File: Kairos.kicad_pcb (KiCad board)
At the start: 2 copper layers, 285 x 94.6 mm, 133 parts, among them Q1 NSS40301MZ4T1G, U1 ATMEGA32U2-AU, Y1 Crystal

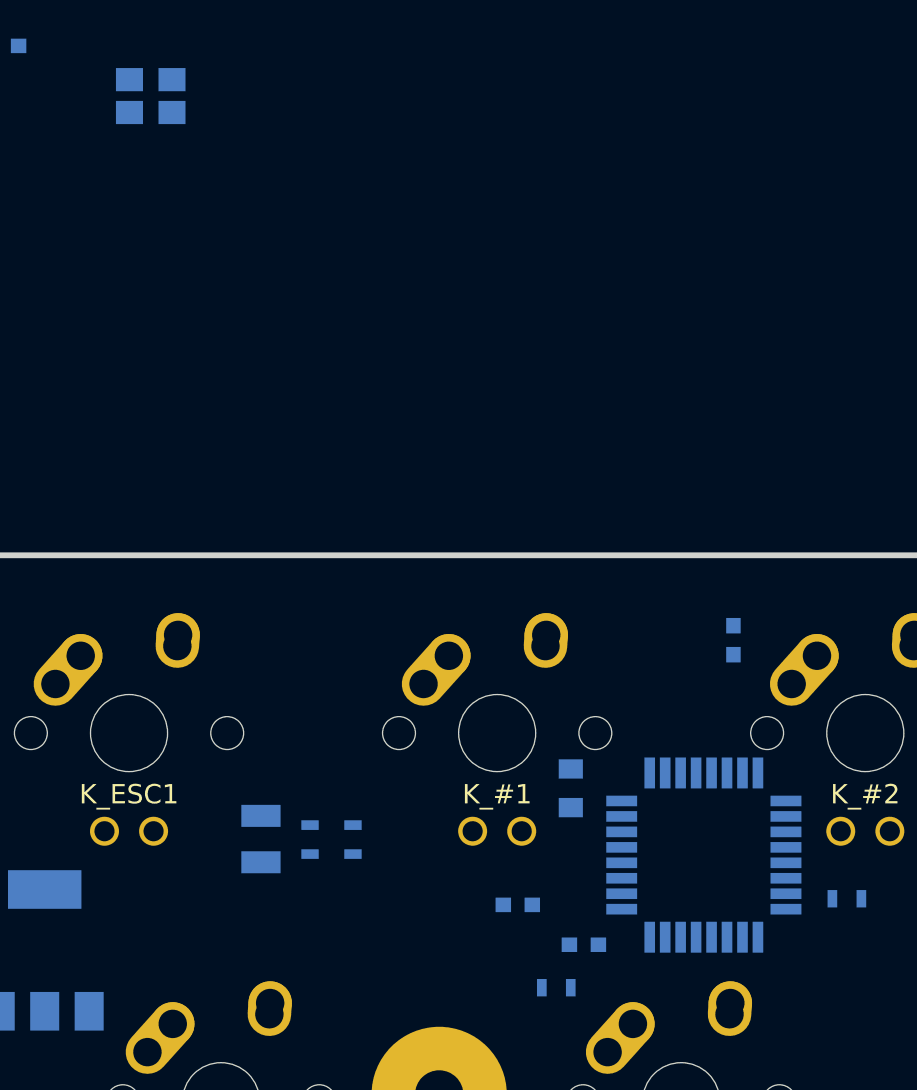
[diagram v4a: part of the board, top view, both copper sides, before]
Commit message: Seems like the crystal pinout is incorrect
Commit before fix for the sake of safety
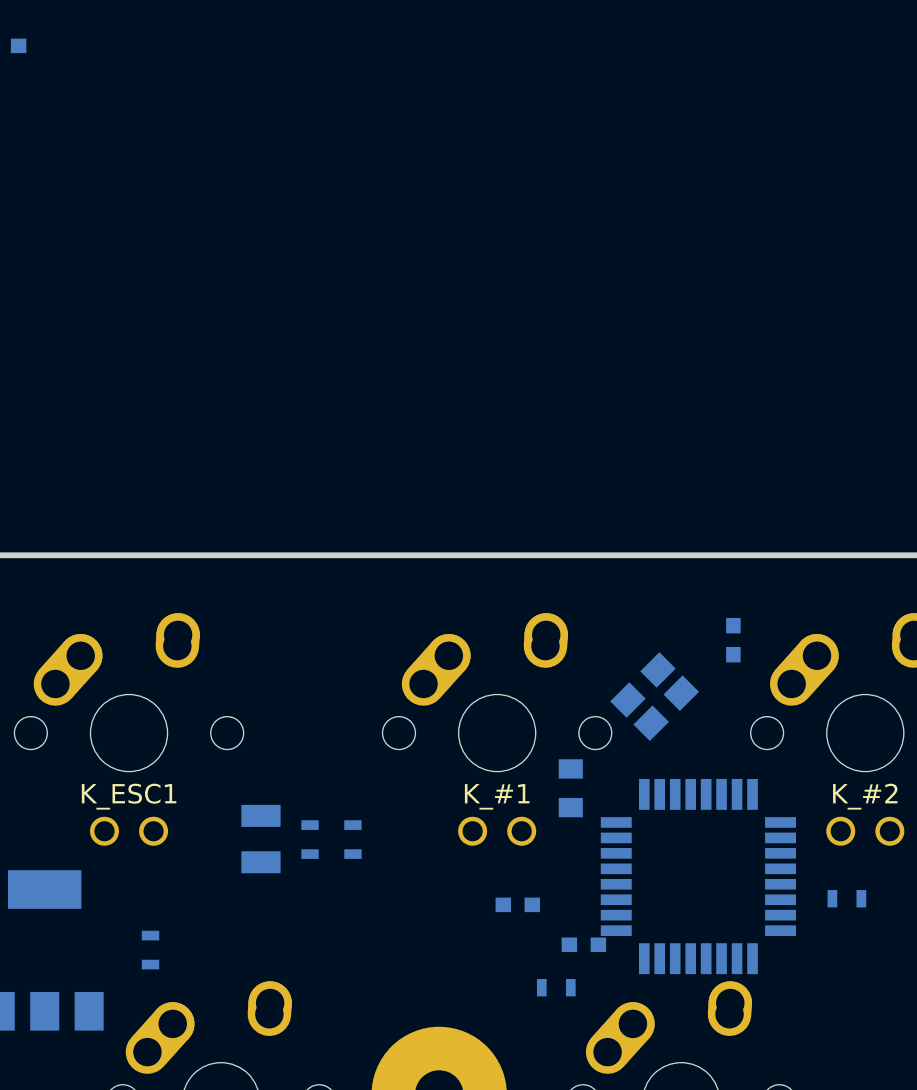
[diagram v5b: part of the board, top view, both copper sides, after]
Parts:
- added R5: 1.5k, Resistors_SMD:R_0603, B.Cu at (15.4, 42.2)
- moved Y1 40.6 mm to (41.5, 29.1), turned to 45 degrees
- moved U1 1.15 mm to (43.8, 38.4)
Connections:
- U1 pad 21: Net-(Q1-Pad1) -> Net-(R5-Pad2)
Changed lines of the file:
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@@
 (kicad_pcb (version 4) (host pcbnew 4.0.6)
   (general
-    (links 590)
-    (no_connects 345)
+    (links 591)
+    (no_connects 347)
     (area 0 0 0 0)
     (thickness 1.6)
@@
     (tracks 0)
     (zones 0)
-    (modules 133)
-    (nets 181)
+    (modules 134)
+    (nets 182)
   )
   (page A4)
@@
   (net 179 "Net-(U1-Pad25)")
   (net 180 "Net-(U1-Pad26)")
+  (net 181 "Net-(R5-Pad2)")
   (net_class Default "This is the default net class."
     (clearance 0.2)
@@
     (add_net "Net-(R3-Pad1)")
     (add_net "Net-(R4-Pad1)")
+    (add_net "Net-(R5-Pad2)")
     (add_net "Net-(U1-Pad10)")
     (add_net "Net-(U1-Pad11)")
@@
   )
   (module Housings_QFP:TQFP-32_7x7mm_Pitch0.8mm (layer B.Cu)
-    (at 44.03125 37.27 270)
+    (at 43.75125 38.38125 270)
     (descr "32-Lead Plastic Thin Quad Flatpack (PT) - 7x7x1.0 mm Body, 2.00 mm [TQFP] (see Microchip Packaging Specification 00000049BS.pdf)")
     (tags "QFP 0.8")
@@
       (net 176 RGBLED))
     (pad 21 smd rect (at 4.25 0.4 270) (size 1.6 0.55) (layers B.Cu B.Paste B.Mask)
-      (net 161 "Net-(Q1-Pad1)"))
+      (net 181 "Net-(R5-Pad2)"))
     (pad 22 smd rect (at 4.25 1.2 270) (size 1.6 0.55) (layers B.Cu B.Paste B.Mask)
       (net 177 "Net-(U1-Pad22)"))
@@
   )
   (module Crystals:Crystal_SMD_3225-4pin_3.2x2.5mm (layer B.Cu)
-    (at 15.41 -2.0075)
+    (at 41.483642 29.069277 45)
     (descr "SMD Crystal SERIES SMD3225/4 http://www.txccrystal.com/images/pdf/7m-accuracy.pdf, 3.2x2.5mm^2 package")
     (tags "SMD SMT crystal")
     (attr smd)
-    (fp_text reference Y1 (at 0 2.45) (layer B.SilkS)
+    (fp_text reference Y1 (at 0 2.45 45) (layer B.SilkS)
       (effects (font (size 1 1) (thickness 0.15)) (justify mirror))
     )
-    (fp_text value Crystal (at 0 -2.45) (layer B.Fab)
+    (fp_text value Crystal (at 0 -2.45 45) (layer B.Fab)
       (effects (font (size 1 1) (thickness 0.15)) (justify mirror))
     )
-    (fp_text user %R (at 0 0) (layer B.Fab)
+    (fp_text user %R (at 0 0 45) (layer B.Fab)
       (effects (font (size 0.7 0.7) (thickness 0.105)) (justify mirror))
     )
@@
     (fp_line (start 2.1 -1.7) (end 2.1 1.7) (layer B.CrtYd) (width 0.05))
     (fp_line (start 2.1 1.7) (end -2.1 1.7) (layer B.CrtYd) (width 0.05))
-    (pad 1 smd rect (at -1.1 -0.85) (size 1.4 1.2) (layers B.Cu B.Paste B.Mask)
+    (pad 1 smd rect (at -1.1 -0.85 45) (size 1.4 1.2) (layers B.Cu B.Paste B.Mask)
       (net 160 "Net-(C6-Pad1)"))
-    (pad 2 smd rect (at 1.1 -0.85) (size 1.4 1.2) (layers B.Cu B.Paste B.Mask)
+    (pad 2 smd rect (at 1.1 -0.85 45) (size 1.4 1.2) (layers B.Cu B.Paste B.Mask)
       (net 159 "Net-(C5-Pad1)"))
-    (pad 3 smd rect (at 1.1 0.85) (size 1.4 1.2) (layers B.Cu B.Paste B.Mask))
-    (pad 4 smd rect (at -1.1 0.85) (size 1.4 1.2) (layers B.Cu B.Paste B.Mask))
+    (pad 3 smd rect (at 1.1 0.85 45) (size 1.4 1.2) (layers B.Cu B.Paste B.Mask))
+    (pad 4 smd rect (at -1.1 0.85 45) (size 1.4 1.2) (layers B.Cu B.Paste B.Mask))
     (model ${KISYS3DMOD}/Crystals.3dshapes/Crystal_SMD_3225-4pin_3.2x2.5mm.wrl
       (at (xyz 0 0 0))
       (scale (xyz 1 1 1))
+      (rotate (xyz 0 0 0))
+    )
+  )
+  (module Resistors_SMD:R_0603 (layer B.Cu)
+    (at 15.39875 42.18375 90)
+    (descr "Resistor SMD 0603, reflow soldering, Vishay (see dcrcw.pdf)")
+    (tags "resistor 0603")
+    (attr smd)
+    (fp_text reference R5 (at 0 1.45 90) (layer B.SilkS)
+      (effects (font (size 1 1) (thickness 0.15)) (justify mirror))
+    )
+    (fp_text value 1.5k (at 0 -1.5 90) (layer B.Fab)
+      (effects (font (size 1 1) (thickness 0.15)) (justify mirror))
+    )
+    (fp_text user %R (at 0 0 90) (layer B.Fab)
+      (effects (font (size 0.5 0.5) (thickness 0.075)) (justify mirror))
+    )
+    (fp_line (start -0.8 -0.4) (end -0.8 0.4) (layer B.Fab) (width 0.1))
+    (fp_line (start 0.8 -0.4) (end -0.8 -0.4) (layer B.Fab) (width 0.1))
+    (fp_line (start 0.8 0.4) (end 0.8 -0.4) (layer B.Fab) (width 0.1))
+    (fp_line (start -0.8 0.4) (end 0.8 0.4) (layer B.Fab) (width 0.1))
+    (fp_line (start 0.5 -0.68) (end -0.5 -0.68) (layer B.SilkS) (width 0.12))
+    (fp_line (start -0.5 0.68) (end 0.5 0.68) (layer B.SilkS) (width 0.12))
+    (fp_line (start -1.25 0.7) (end 1.25 0.7) (layer B.CrtYd) (width 0.05))
+    (fp_line (start -1.25 0.7) (end -1.25 -0.7) (layer B.CrtYd) (width 0.05))
+    (fp_line (start 1.25 -0.7) (end 1.25 0.7) (layer B.CrtYd) (width 0.05))
+    (fp_line (start 1.25 -0.7) (end -1.25 -0.7) (layer B.CrtYd) (width 0.05))
+    (pad 1 smd rect (at -0.75 0 90) (size 0.5 0.9) (layers B.Cu B.Paste B.Mask)
+      (net 161 "Net-(Q1-Pad1)"))
+    (pad 2 smd rect (at 0.75 0 90) (size 0.5 0.9) (layers B.Cu B.Paste B.Mask)
+      (net 181 "Net-(R5-Pad2)"))
+    (model ${KISYS3DMOD}/Resistors_SMD.3dshapes/R_0603.wrl
+      (at (xyz 0 0 0))
+      (scale (xyz 1 1 1))

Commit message: Finish controller area
Poof
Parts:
- Y1: value Crystal -> Crystal_GND24
- moved C6 47.2 mm to (40.3, 24.3), turned to 90 degrees
- moved C5 45.0 mm to (42.4, 24.3), turned to 90 degrees
- moved C1 2.43 mm to (35.4, 41.4)
- moved C2 1.81 mm to (35.5, 38.4), turned to 180 degrees
- moved C4 0.80 mm to (37.1, 33.0), turned to 180 degrees
- moved U1 0.79 mm to (43.8, 37.6)
- moved R1 0.77 mm to (51.9, 38.9)
- moved R4 0.48 mm to (36.9, 44.1)
- moved Y1 0.20 mm to (41.3, 28.9)
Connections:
- Y1 pad 2: Net-(C5-Pad1) -> GND
- Y1 pad 3: (no net) -> Net-(C5-Pad1)
- Y1 pad 4: (no net) -> GND
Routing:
- net GND: track 0.00 -> 72.2 mm, vias 0 -> 5
- net +5V: track 0.00 -> 50.2 mm, vias 0 -> 2
- net Net-(R2-Pad1): track 0.00 -> 18.4 mm
- net Net-(R3-Pad1): track 0.00 -> 16.2 mm
- net Net-(C6-Pad1): track 0.00 -> 8.86 mm
- net LEDGND: track 0.00 -> 6.30 mm
- net Net-(C5-Pad1): track 0.00 -> 4.97 mm
- net Net-(R4-Pad1): track 0.00 -> 4.59 mm
- net Net-(C1-Pad1): track 0.00 -> 4.53 mm
- net Net-(Q1-Pad1): track 0.00 -> 4.47 mm
- net Net-(R1-Pad2): track 0.00 -> 3.49 mm
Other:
- net class HighCurrent added: clearance 0.2, trace_width 0.381, via_dia 0.6, via_drill 0.4

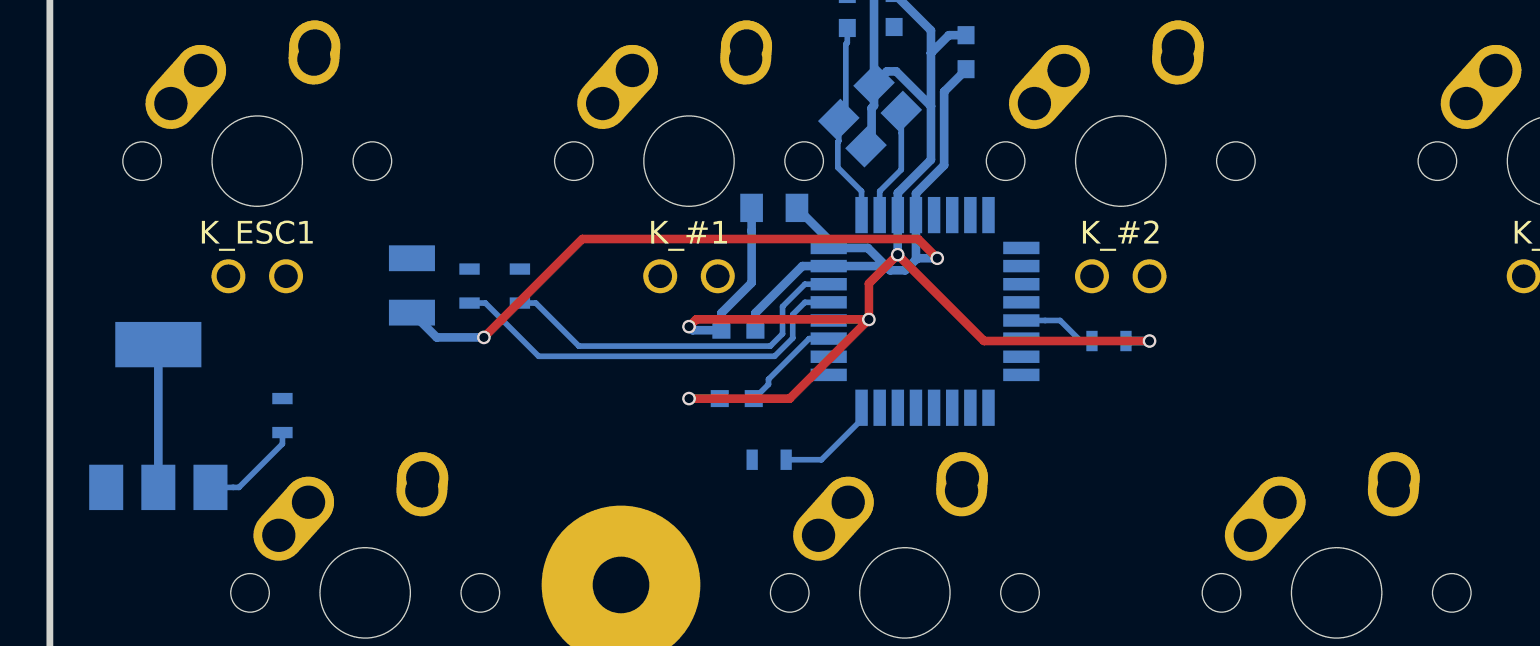
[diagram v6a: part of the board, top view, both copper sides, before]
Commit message: Adjust transistor location
Last one was too close to board edge
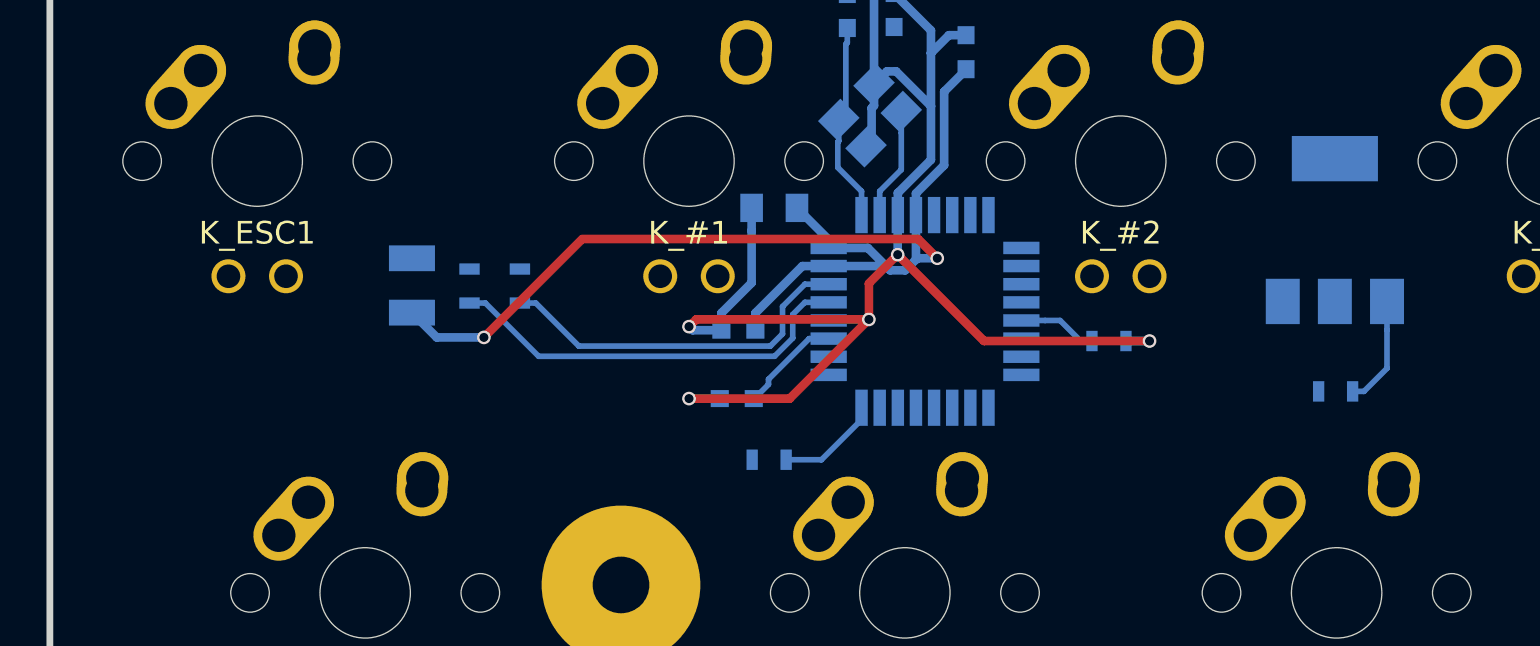
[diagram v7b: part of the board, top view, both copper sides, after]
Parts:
- moved Q1 52.6 mm to (61.8, 34.0)
- moved R5 46.5 mm to (61.9, 41.1), turned to 180 degrees
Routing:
- net LEDGND: track 6.30 -> 0.00 mm
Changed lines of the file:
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@@
   (general
     (links 593)
-    (no_connects 349)
-    (area 0 0 0 0)
+    (no_connects 323)
+    (area 4.44875 21.156249 290.787501 120.63125)
     (thickness 1.6)
     (drawings 0)
-    (tracks 118)
+    (tracks 117)
     (zones 0)
     (modules 134)
@@
   )
   (module TO_SOT_Packages_SMD:SOT-223-3Lead_TabPin2 (layer B.Cu)
-    (at 9.92375 42.2025 90)
+    (at 61.835 33.9975 90)
     (descr "module CMS SOT223 4 pins")
     (tags "CMS SOT")
@@
   )
   (module Resistors_SMD:R_0603 (layer B.Cu)
-    (at 15.39875 42.18375 90)
+    (at 61.86875 41.11625 180)
     (descr "Resistor SMD 0603, reflow soldering, Vishay (see dcrcw.pdf)")
     (tags "resistor 0603")
     (attr smd)
-    (fp_text reference R5 (at 0 1.45 90) (layer B.SilkS)
+    (fp_text reference R5 (at 0 1.45 180) (layer B.SilkS)
       (effects (font (size 1 1) (thickness 0.15)) (justify mirror))
     )
-    (fp_text value 1.5k (at 0 -1.5 90) (layer B.Fab)
+    (fp_text value 1.5k (at 0 -1.5 180) (layer B.Fab)
       (effects (font (size 1 1) (thickness 0.15)) (justify mirror))
     )
-    (fp_text user %R (at 0 0 90) (layer B.Fab)
+    (fp_text user %R (at 0 0 180) (layer B.Fab)
       (effects (font (size 0.5 0.5) (thickness 0.075)) (justify mirror))
     )
@@
     (fp_line (start 1.25 -0.7) (end 1.25 0.7) (layer B.CrtYd) (width 0.05))
     (fp_line (start 1.25 -0.7) (end -1.25 -0.7) (layer B.CrtYd) (width 0.05))
-    (pad 1 smd rect (at -0.75 0 90) (size 0.5 0.9) (layers B.Cu B.Paste B.Mask)
+    (pad 1 smd rect (at -0.75 0 180) (size 0.5 0.9) (layers B.Cu B.Paste B.Mask)
       (net 161 "Net-(Q1-Pad1)"))
-    (pad 2 smd rect (at 0.75 0 90) (size 0.5 0.9) (layers B.Cu B.Paste B.Mask)
+    (pad 2 smd rect (at 0.75 0 180) (size 0.5 0.9) (layers B.Cu B.Paste B.Mask)
       (net 181 "Net-(R5-Pad2)"))
     (model ${KISYS3DMOD}/Resistors_SMD.3dshapes/R_0603.wrl
@@
     )
   )
-  (segment (start 9.92375 45.3525) (end 9.92375 39.0525) (width 0.381) (layer B.Cu) (net 4))
   (segment (start 36.195 41.43375) (end 36.22 41.43375) (width 0.25) (layer B.Cu) (net 139))
   (segment (start 36.22 41.43375) (end 36.845 40.80875) (width 0.25) (layer B.Cu) (net 139))
@@
   (segment (start 39.903866 30.109865) (end 39.946034 30.067697) (width 0.25) (layer B.Cu) (net 160))
   (segment (start 39.946034 30.067697) (end 39.946034 29.119169) (width 0.25) (layer B.Cu) (net 160))
-  (segment (start 15.39875 42.93375) (end 15.39875 43.43375) (width 0.25) (layer B.Cu) (net 161))
-  (segment (start 15.39875 43.43375) (end 13.48 45.3525) (width 0.25) (layer B.Cu) (net 161))
-  (segment (start 13.48 45.3525) (end 13.22375 45.3525) (width 0.25) (layer B.Cu) (net 161))
-  (segment (start 13.22375 45.3525) (end 12.22375 45.3525) (width 0.25) (layer B.Cu) (net 161))
+  (segment (start 62.61875 41.11625) (end 63.11875 41.11625) (width 0.25) (layer B.Cu) (net 161))
+  (segment (start 63.11875 41.11625) (end 64.135 40.1) (width 0.25) (layer B.Cu) (net 161))
+  (segment (start 64.135 40.1) (end 64.135 38.3975) (width 0.25) (layer B.Cu) (net 161))
+  (segment (start 64.135 38.3975) (end 64.135 37.1475) (width 0.25) (layer B.Cu) (net 161))
 )
